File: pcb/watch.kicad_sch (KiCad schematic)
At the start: 0 parts

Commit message: Placing ESP32-S3-WROOM-1
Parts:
- added U1: ESP32-S3-WROOM-1, RF_Module:ESP32-S3-WROOM-1, symbol RF_Module:ESP32-S3-WROOM-1
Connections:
- new net +3V3: U1.2 (3V3)
- new net GND: U1.1 (GND), U1.40 (GND), U1.41 (GND)
- no-connect marks 0 -> 36

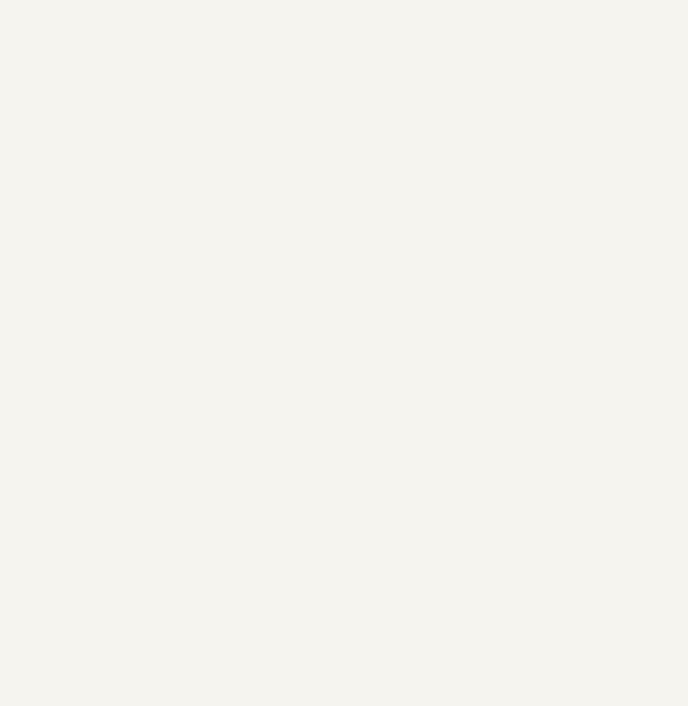
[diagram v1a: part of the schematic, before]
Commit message: Adding USBC schematic
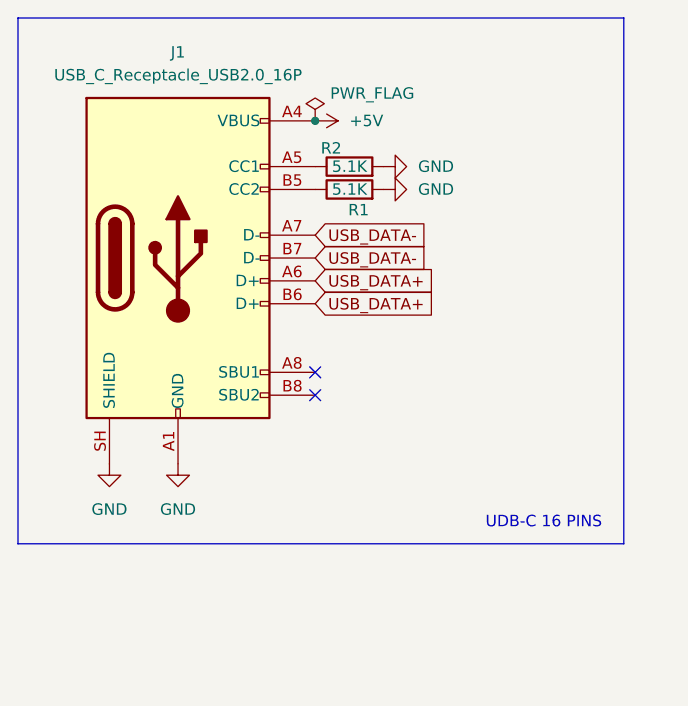
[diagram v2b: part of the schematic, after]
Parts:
- added J1: USB_C_Receptacle_USB2.0_16P, symbol Connector:USB_C_Receptacle_USB2.0_16P
- added R1, R2: 5.1K, symbol Device:R
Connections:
- net GND: now also J1.A1 (GND), J1.A12 (GND), J1.B1 (GND), J1.B12 (GND), J1.SH (SHIELD), R1.2, R2.2
- new net: J1.A5 (CC1), R2.1
- new net: J1.B5 (CC2), R1.1
- new net +5V: J1.A4 (VBUS), J1.A9 (VBUS), J1.B4 (VBUS), J1.B9 (VBUS)
- new net USB_DATA+: J1.A6 (D+), J1.B6 (D+)
- new net USB_DATA-: J1.A7 (D-), J1.B7 (D-)
- no-connect marks 36 -> 38
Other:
- note added: "UDB-C 16 PINS"

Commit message: Adding AMS1117
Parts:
- added U2: AMS1117-3.3, Package_TO_SOT_SMD:SOT-223-3_TabPin2, symbol Regulator_Linear:AMS1117-3.3
- U1: footprint RF_Module:ESP32-S3-WROOM-1 -> RF_Module:ESP32-S3-WROOM-1U
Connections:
- net +3V3: now also U2.2 (VO)
- net +5V: now also U2.3 (VI)
- net GND: now also U2.1 (GND)
